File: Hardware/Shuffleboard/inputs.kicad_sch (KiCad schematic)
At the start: 27 parts

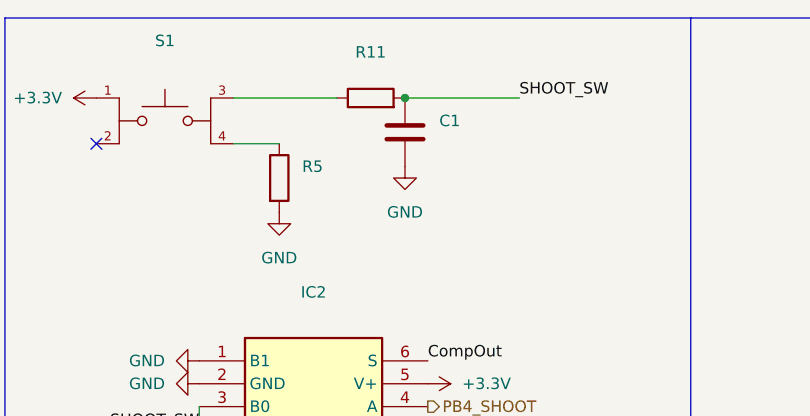
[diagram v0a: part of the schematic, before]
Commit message: tht resistors
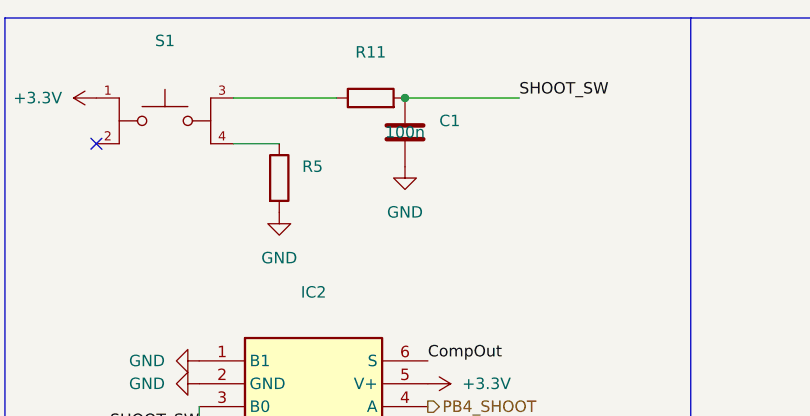
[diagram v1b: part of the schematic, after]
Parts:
- C1, C3, C4, C5, C7: value (none) -> 100n
- D1: value (none) -> Red
- IC1, IC2: Mouser Link google.com/search?q=78-DG3157EDL-T1-GE3&oq=78-DG3157EDL-T1-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 -> https://www.mouser.com/ProductDetail/Vishay-Siliconix/DG315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
- R1, R12, R45, R5, R9: value (none) -> 10k; now left out of the parts list
- R10, R14: value (none) -> 330
- R11, R2, R3, R4, R6: value (none) -> 1k; now left out of the parts list
- R13: value (none) -> 10k; footprint Resistor_SMD:R_0603_1608Metric_Pad0.98x0.95mm_HandSolder -> Resistor_THT:R_Axial_DIN0207_L6.3mm_D2.5mm_P7.62mm_Horizontal; now left out of the parts list
- U3: value (none) -> Comparator

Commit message: updated to end
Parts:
- C1, C3, C4, C5, C7: value 100n -> (none)
- D1: value Red -> (none)
- R1, R12, R13, R45, R5, R9: value 10k -> (none)
- R10, R14: value 330 -> (none)
- R11, R2, R3, R4, R6: value 1k -> (none)
- U3: value Comparator -> (none)
